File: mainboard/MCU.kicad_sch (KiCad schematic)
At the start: 5 parts, among them M901 ESP32-S3-WROOM-1, X901 PROG

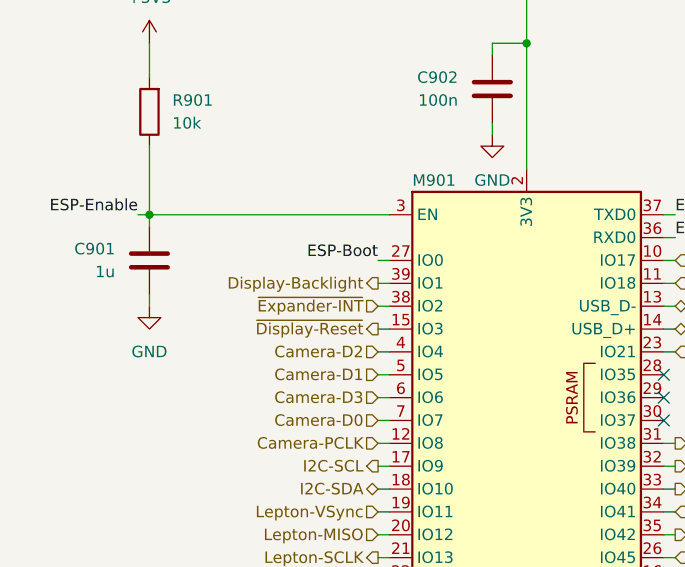
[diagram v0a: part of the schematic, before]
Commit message: Continue routing, add flash LEDs for the RGB camera, add PWM controller for the Display Backlight and the flash LEDs, add Polyfuse for the battery
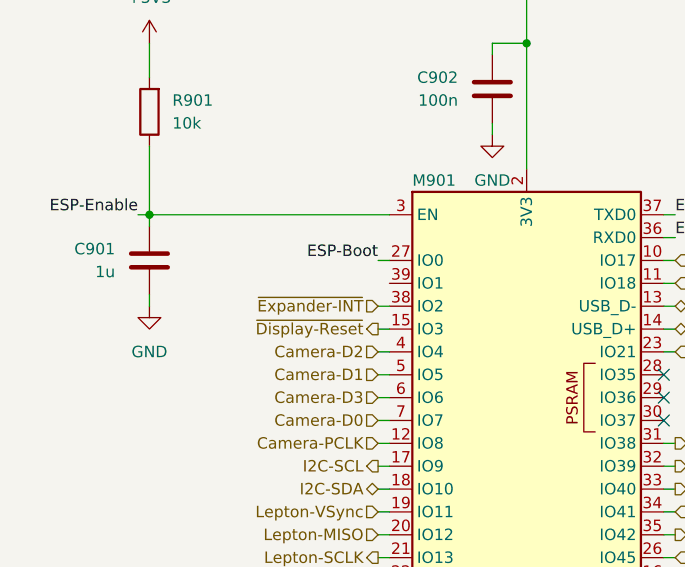
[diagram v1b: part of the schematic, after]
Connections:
- net Display-Backlight: no longer names the net of M901.39 (IO1)
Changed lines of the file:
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@@
-	(wire
-		(pts
-			(xy 121.92 72.39) (xy 123.19 72.39)
-		)
-		(stroke
-			(width 0)
-			(type default)
-		)
-	)
 	(wire
 		(pts
@@
 		(effects
 			(font
-				(size 1.27 1.27)
-			)
-			(justify right)
-		)
-	)
-	(hierarchical_label "Display-Backlight"
-		(shape output)
-		(at 121.92 72.39 180)
-		(effects
-			(font

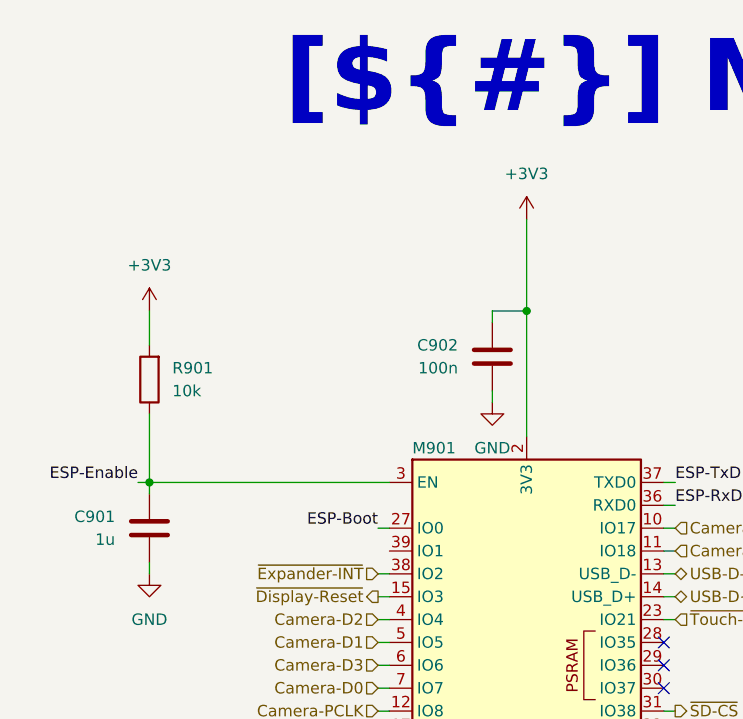
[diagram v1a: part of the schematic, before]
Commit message: Remove ADC for battery measurement and add a fuel gauge
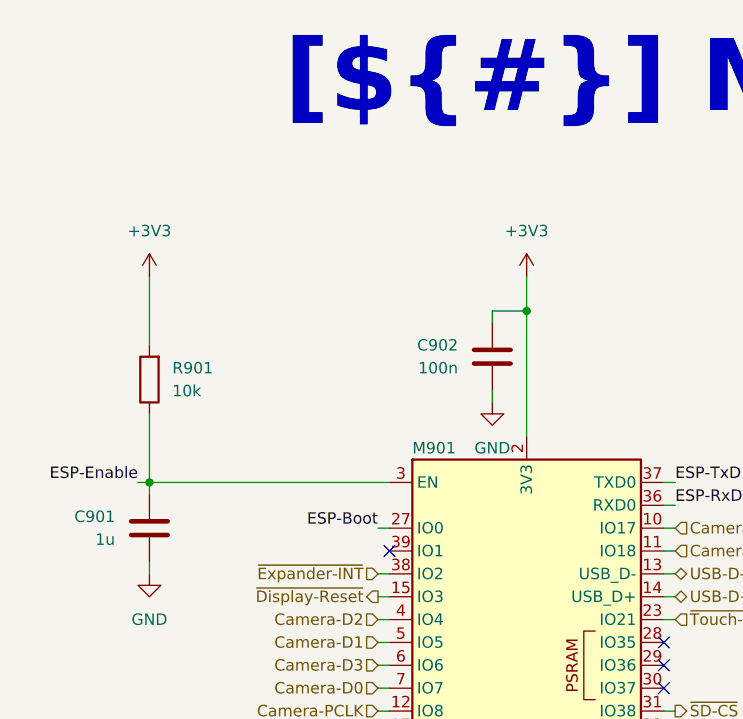
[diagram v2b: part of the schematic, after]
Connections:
- no-connect marks 3 -> 4
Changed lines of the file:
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@@
+	)
+	(no_connect
+		(at 123.19 72.39)
 	)
 	(no_connect
@@
 	(wire
 		(pts
-			(xy 138.43 35.56) (xy 138.43 45.72)
+			(xy 138.43 41.91) (xy 138.43 45.72)
 		)
 		(stroke
@@
 	(wire
 		(pts
-			(xy 96.52 45.72) (xy 96.52 49.53)
+			(xy 96.52 41.91) (xy 96.52 49.53)
 		)
 		(stroke
@@
 	(symbol
 		(lib_id "power:+3V3")
-		(at 138.43 35.56 0)
+		(at 138.43 41.91 0)
 		(unit 1)
 		(exclude_from_sim no)
@@
 		(fields_autoplaced yes)
 		(property "Reference" "#PWR0904"
-			(at 138.43 39.37 0)
+			(at 138.43 45.72 0)
 			(effects
 				(font
@@
 		)
 		(property "Value" "+3V3"
-			(at 138.43 30.48 0)
+			(at 138.43 36.83 0)
 			(effects
 				(font
@@
 		)
 		(property "Footprint" ""
-			(at 138.43 35.56 0)
+			(at 138.43 41.91 0)
 			(effects
 				(font
@@
 		)
 		(property "Datasheet" ""
-			(at 138.43 35.56 0)
+			(at 138.43 41.91 0)
 			(effects
 				(font
@@
 		)
 		(property "Description" "Power symbol creates a global label with name \"+3V3\""
-			(at 138.43 35.56 0)
+			(at 138.43 41.91 0)
 			(effects
 				(font
@@
 	(symbol
 		(lib_id "power:+3V3")
-		(at 96.52 45.72 0)
+		(at 96.52 41.91 0)
 		(unit 1)
 		(exclude_from_sim no)
@@
 		(fields_autoplaced yes)
 		(property "Reference" "#PWR0901"
-			(at 96.52 49.53 0)
+			(at 96.52 45.72 0)
 			(effects
 				(font
@@
 		)
 		(property "Value" "+3V3"
-			(at 96.52 40.64 0)
+			(at 96.52 36.83 0)
 			(effects
 				(font
@@
 		)
 		(property "Footprint" ""
-			(at 96.52 45.72 0)
+			(at 96.52 41.91 0)
 			(effects
 				(font
@@
 		)
 		(property "Datasheet" ""
-			(at 96.52 45.72 0)
+			(at 96.52 41.91 0)
 			(effects
 				(font
@@
 		)
 		(property "Description" "Power symbol creates a global label with name \"+3V3\""
-			(at 96.52 45.72 0)
-			(effects
-				(font
+			(at 96.52 41.91 0)
+			(effects
+				(font

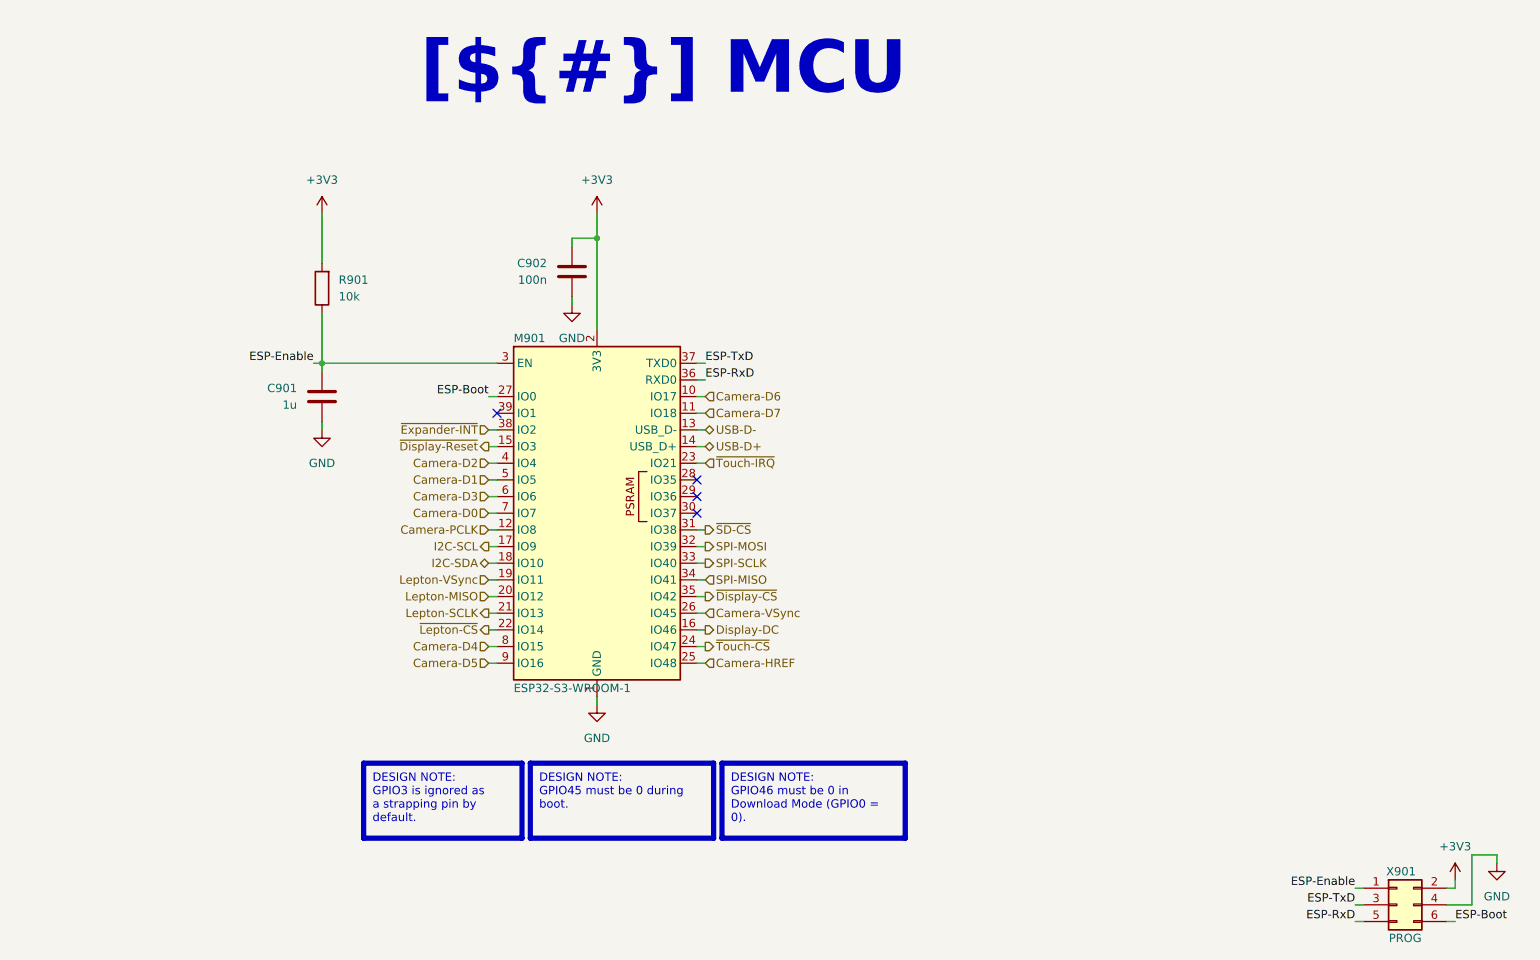
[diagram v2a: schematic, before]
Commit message: New position for display connector
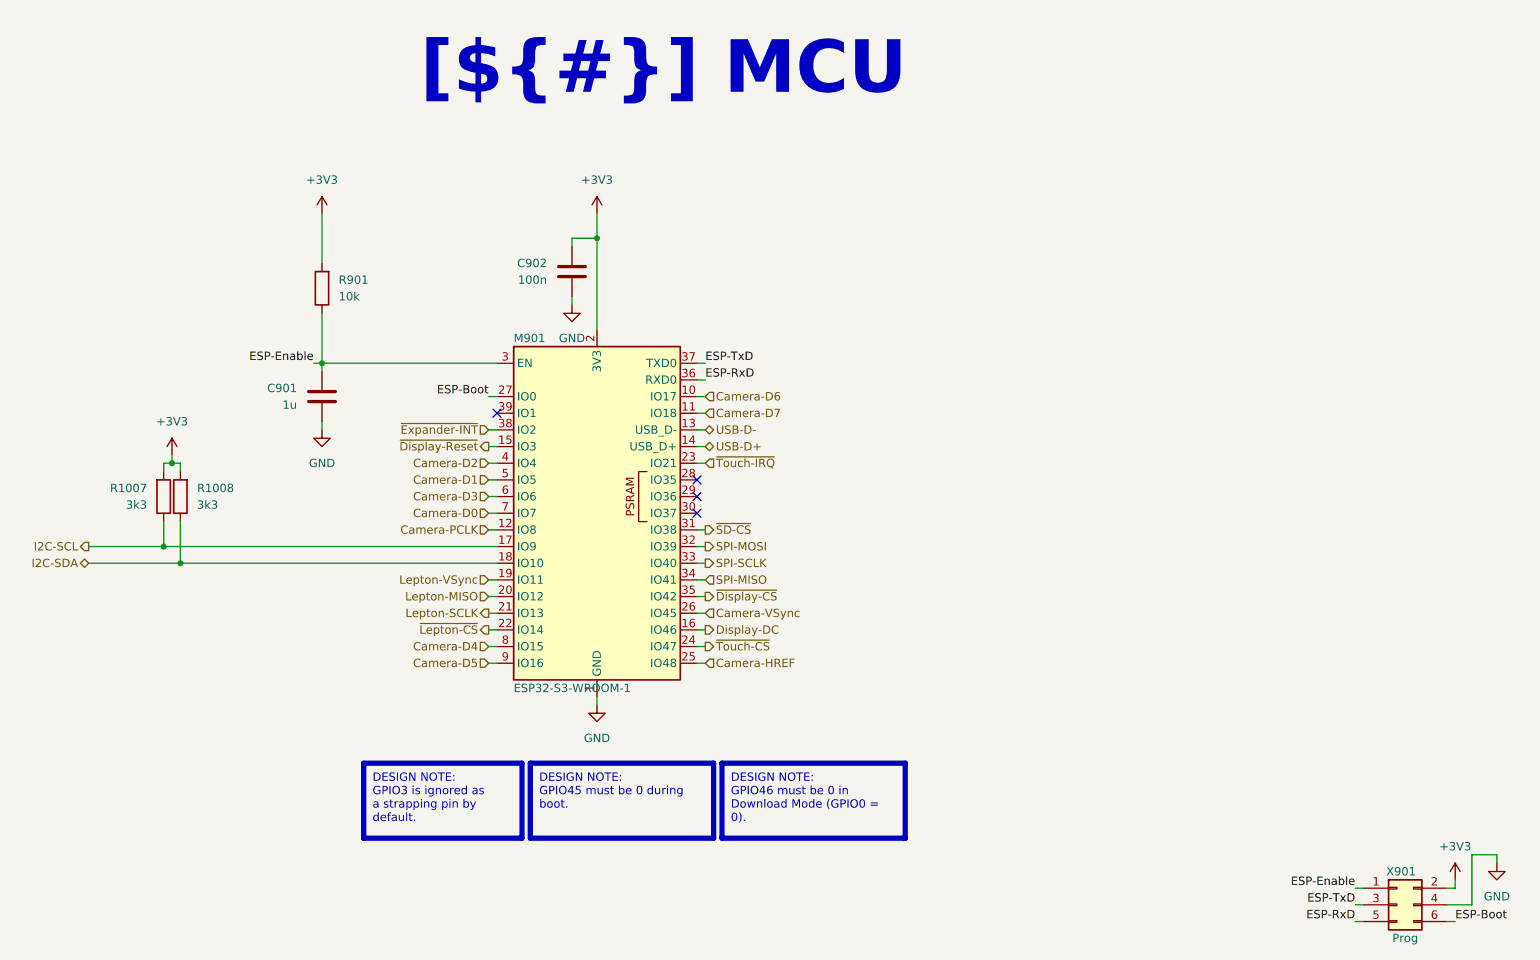
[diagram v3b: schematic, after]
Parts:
- added R1007, R1008: 3k3, Resistor_SMD:R_0603_1608Metric, symbol Device:R
- X901: value PROG -> Prog
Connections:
- net +3V3: now also R1007.2, R1008.2
- net I2C-SCL: now also R1007.1
- net I2C-SDA: now also R1008.1

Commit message: Layout complete
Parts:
- renumbered R1007 to R901, R1008 to R902, R901 to R903
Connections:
- net ~{Expander-Int}: now reaches M901.39 (IO1)
- net ~{Expander-INT} renamed ~{Display-Expander-Int}
- net ~{Touch-CS} renamed ~{Touch-Reset}
- no-connect marks 4 -> 3
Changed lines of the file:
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@@
 		(exclude_from_sim no)
 		(at 12.7 12.7 0)
-		(size 271.78 13.97)
+		(size 271.78 20.32)
 		(margins 5.9999 5.9999 5.9999 5.9999)
 		(stroke
@@
 	)
 	(no_connect
-		(at 123.19 72.39)
-	)
-	(no_connect
 		(at 153.67 87.63)
 	)
@@
 		(pts
 			(xy 153.67 90.17) (xy 154.94 90.17)
+		)
+		(stroke
+			(width 0)
+			(type default)
+		)
+	)
+	(wire
+		(pts
+			(xy 121.92 72.39) (xy 123.19 72.39)
 		)
 		(stroke
@@
 		)
 	)
+	(hierarchical_label "~{Display-Expander-Int}"
+		(shape input)
+		(at 121.92 74.93 180)
+		(effects
+			(font
+				(size 1.27 1.27)
+			)
+			(justify right)
+		)
+	)
 	(hierarchical_label "Camera-PCLK"
 		(shape input)
@@
 		)
 	)
-	(hierarchical_label "~{Expander-INT}"
+	(hierarchical_label "~{Expander-Int}"
 		(shape input)
-		(at 121.92 74.93 180)
+		(at 121.92 72.39 180)
 		(effects
 			(font
@@
 		)
 	)
-	(hierarchical_label "~{Touch-CS}"
+	(hierarchical_label "~{Touch-Reset}"
 		(shape output)
 		(at 154.94 107.95 0)
@@
 		(dnp no)
 		(fields_autoplaced yes)
-		(property "Reference" "#PWR0903"
+		(property "Reference" "#PWR0904"
 			(at 134.62 62.23 0)
 			(effects
@@
 			(project "Thermal Cam"
 				(path "/d5742f03-3b1a-42e5-a384-018bd4b919aa/c5103ceb-5325-4a84-a025-9638a412984e/85a410e7-e905-4760-8407-37aaa1389258"
-					(reference "#PWR0903")
+					(reference "#PWR0904")
 					(unit 1)
 				)
@@
 		(on_board yes)
 		(dnp no)
-		(property "Reference" "R1007"
+		(property "Reference" "R901"
 			(at 69.85 83.82 0)
 			(effects
@@
 			(project "Mainboard"
 				(path "/d5742f03-3b1a-42e5-a384-018bd4b919aa/c5103ceb-5325-4a84-a025-9638a412984e/85a410e7-e905-4760-8407-37aaa1389258"
-					(reference "R1007")
+					(reference "R901")
 					(unit 1)
 				)
@@
 		(dnp no)
 		(fields_autoplaced yes)
-		(property "Reference" "#PWR0907"
+		(property "Reference" "#PWR0908"
 			(at 275.59 147.32 0)
 			(effects
@@
 			(project "Thermal Cam"
 				(path "/d5742f03-3b1a-42e5-a384-018bd4b919aa/c5103ceb-5325-4a84-a025-9638a412984e/85a410e7-e905-4760-8407-37aaa1389258"
-					(reference "#PWR0907")
+					(reference "#PWR0908")
 					(unit 1)
 				)
@@
 		(dnp no)
 		(fields_autoplaced yes)
-		(property "Reference" "#PWR0906"
+		(property "Reference" "#PWR0907"
 			(at 269.24 147.32 0)
 			(effects
@@
 			(project "Thermal Cam"
 				(path "/d5742f03-3b1a-42e5-a384-018bd4b919aa/c5103ceb-5325-4a84-a025-9638a412984e/85a410e7-e905-4760-8407-37aaa1389258"
-					(reference "#PWR0906")
+					(reference "#PWR0907")
 					(unit 1)
 				)
@@
 		(on_board yes)
 		(dnp no)
-		(property "Reference" "R1008"
+		(property "Reference" "R902"
 			(at 77.47 83.82 0)
 			(effects
@@
 			(project "Mainboard"
 				(path "/d5742f03-3b1a-42e5-a384-018bd4b919aa/c5103ceb-5325-4a84-a025-9638a412984e/85a410e7-e905-4760-8407-37aaa1389258"
-					(reference "R1008")
+					(reference "R902")
 					(unit 1)
 				)
@@
 		(dnp no)
 		(fields_autoplaced yes)
-		(property "Reference" "R901"
+		(property "Reference" "R903"
 			(at 99.06 52.0699 0)
 			(effects
@@
 			(project "Thermal Cam"
 				(path "/d5742f03-3b1a-42e5-a384-018bd4b919aa/c5103ceb-5325-4a84-a025-9638a412984e/85a410e7-e905-4760-8407-37aaa1389258"
-					(reference "R901")
+					(reference "R903")
 					(unit 1)
 				)
@@
 		(dnp no)
 		(fields_autoplaced yes)
-		(property "Reference" "#PWR0904"
+		(property "Reference" "#PWR0905"
 			(at 138.43 45.72 0)
 			(effects
@@
 			(project "Thermal Cam"
 				(path "/d5742f03-3b1a-42e5-a384-018bd4b919aa/c5103ceb-5325-4a84-a025-9638a412984e/85a410e7-e905-4760-8407-37aaa1389258"
-					(reference "#PWR0904")
+					(reference "#PWR0905")
 					(unit 1)
 				)
@@
 		(dnp no)
 		(fields_autoplaced yes)
-		(property "Reference" "#PWR0901"
+		(property "Reference" "#PWR0902"
 			(at 96.52 45.72 0)
 			(effects
@@
 			(project "Thermal Cam"
 				(path "/d5742f03-3b1a-42e5-a384-018bd4b919aa/c5103ceb-5325-4a84-a025-9638a412984e/85a410e7-e905-4760-8407-37aaa1389258"
-					(reference "#PWR0901")
+					(reference "#PWR0902")
 					(unit 1)
 				)
@@
 		(dnp no)
 		(fields_autoplaced yes)
-		(property "Reference" "#PWR0902"
+		(property "Reference" "#PWR0903"
 			(at 96.52 81.28 0)
 			(effects
@@
 			(project "Thermal Cam"
 				(path "/d5742f03-3b1a-42e5-a384-018bd4b919aa/c5103ceb-5325-4a84-a025-9638a412984e/85a410e7-e905-4760-8407-37aaa1389258"
-					(reference "#PWR0902")
+					(reference "#PWR0903")
 					(unit 1)
 				)
@@
 		(dnp no)
 		(fields_autoplaced yes)
-		(property "Reference" "#PWR0905"
+		(property "Reference" "#PWR0906"
 			(at 138.43 123.19 0)
 			(effects
@@
 			(project "Thermal Cam"
 				(path "/d5742f03-3b1a-42e5-a384-018bd4b919aa/c5103ceb-5325-4a84-a025-9638a412984e/85a410e7-e905-4760-8407-37aaa1389258"
-					(reference "#PWR0905")
+					(reference "#PWR0906")
 					(unit 1)
 				)
@@
 		(dnp no)
 		(fields_autoplaced yes)
-		(property "Reference" "#PWR01013"
+		(property "Reference" "#PWR0901"
 			(at 73.66 82.55 0)
 			(effects
@@
 			(project "Mainboard"
 				(path "/d5742f03-3b1a-42e5-a384-018bd4b919aa/c5103ceb-5325-4a84-a025-9638a412984e/85a410e7-e905-4760-8407-37aaa1389258"
-					(reference "#PWR01013")
-					(unit 1)
-				)
+					(reference "#PWR0901")
+					(unit 1)
+				)

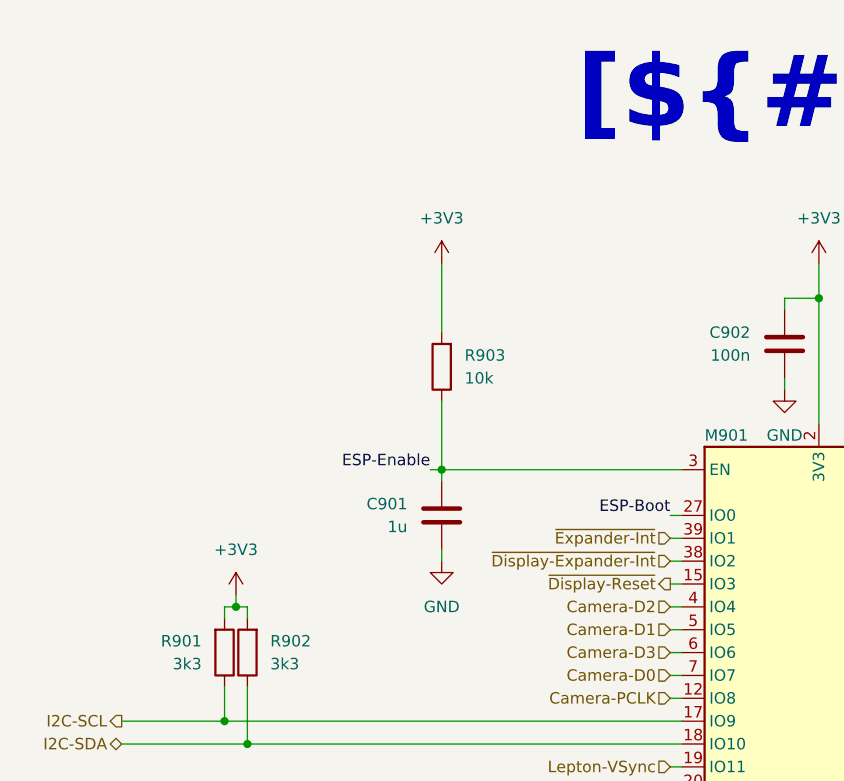
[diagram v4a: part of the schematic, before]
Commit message: Add reset switch
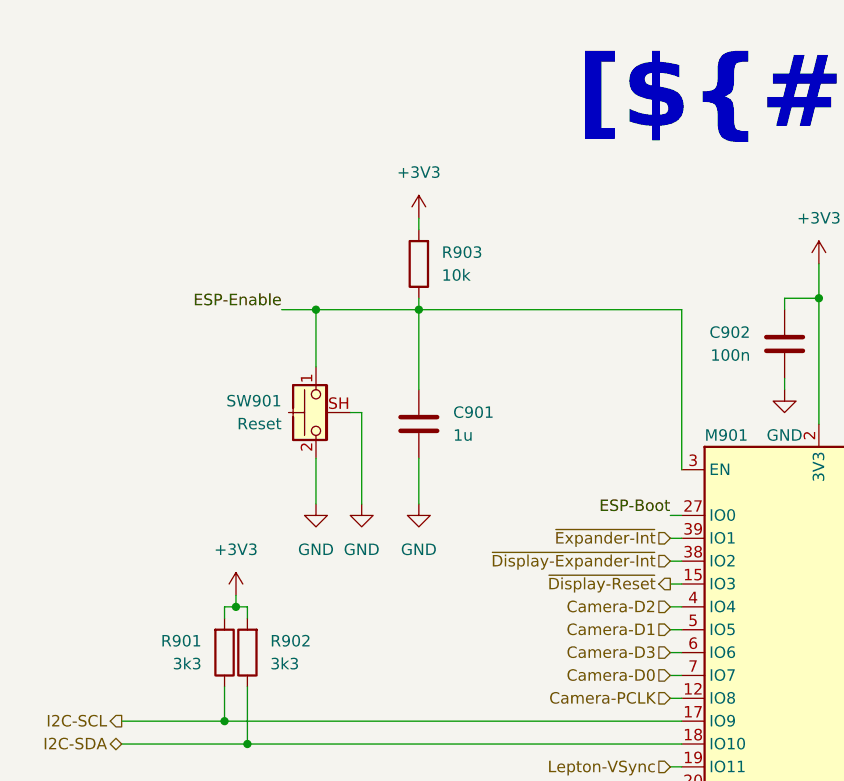
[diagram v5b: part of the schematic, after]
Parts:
- added SW901: Reset, Same Sky:TS11, symbol Switch:SW_Push_Shielded
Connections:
- net ESP-Enable: now also SW901.1
- net GND: now also SW901.2, SW901.SH (B)
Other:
- moved on the sheet: C901, R903

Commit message: Task: Issue #7
- Increase the width of the cutout for the temperature sensor
- Add missing component informations
- Fix wrong component informations

Closes: #7

Signed-off-by: Daniel Kampert <DanielKampert@kampis-elektroecke.de>
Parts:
- R903: manf Bourns -> YAGEO; manf# CR0603-JW-103ELF -> RC0603FR-073K3L; mouser# 652-CR0603-JW-103ELF -> 603-RC0603FR-073K3L
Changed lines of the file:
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@@
 			)
 		)
-		(property "manf" "Bourns"
+		(property "manf" "YAGEO"
 			(at 93.98 41.91 0)
 			(effects
@@
 			)
 		)
-		(property "manf#" "CR0603-JW-103ELF"
+		(property "manf#" "RC0603FR-073K3L"
 			(at 93.98 41.91 0)
 			(effects
@@
 			)
 		)
-		(property "mouser#" "652-CR0603-JW-103ELF"
+		(property "mouser#" "603-RC0603FR-073K3L"
 			(at 93.98 41.91 0)
 			(effects

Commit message: Bug: Fixing several component issues
Closes: #17
Closes: #16
Closes: #15
Closes: #14
Closes: #13
Closes: #12

Signed-off-by: Daniel Kampert <danielkampert@kampis-elektroecke.de>
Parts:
- SW901: manf# TS11-674-50-BK-260-RA-D -> TS11-674-43-BK-260-RA-D; mouser# 179-TS1167450260RAD -> 179-TS1167443260RAD
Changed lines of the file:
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@@
 			)
 		)
-		(property "manf#" "TS11-674-50-BK-260-RA-D"
+		(property "manf#" "TS11-674-43-BK-260-RA-D"
 			(at 82.55 58.42 0)
 			(effects
@@
 			)
 		)
-		(property "mouser#" "179-TS1167450260RAD"
+		(property "mouser#" "179-TS1167443260RAD"
 			(at 82.55 58.42 0)
 			(effects
